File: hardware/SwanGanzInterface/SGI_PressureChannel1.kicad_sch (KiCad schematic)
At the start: 17 parts, among them U4 INA122D, U5 OPA2350

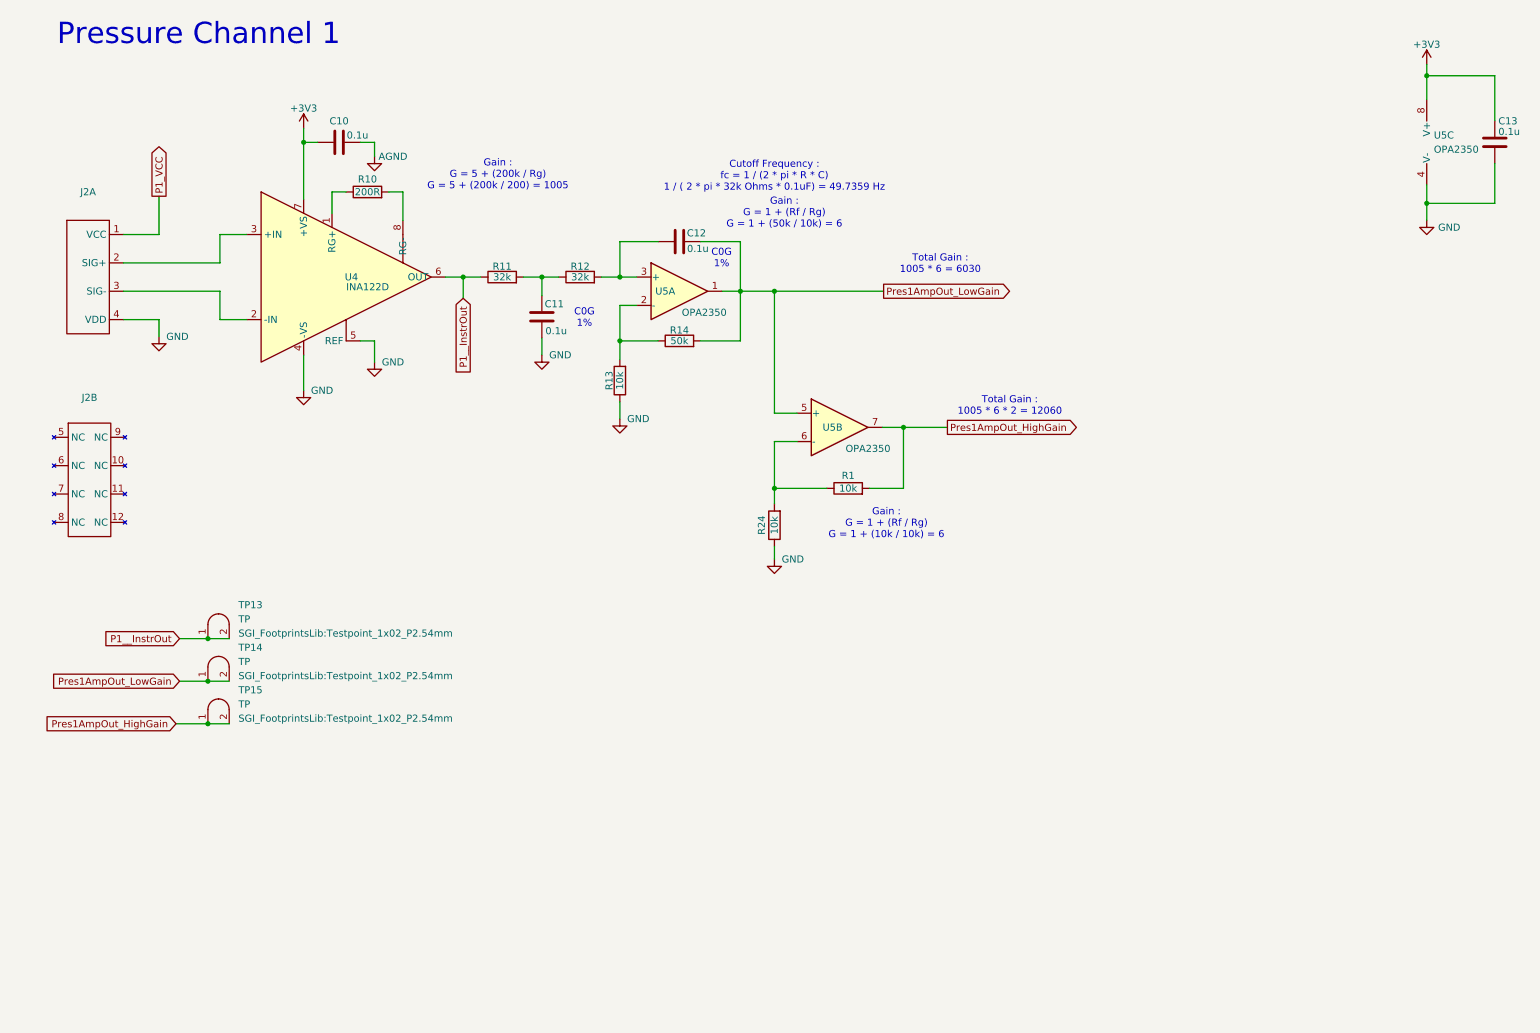
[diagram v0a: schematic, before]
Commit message: Routed Microcontroller Schematic Pins
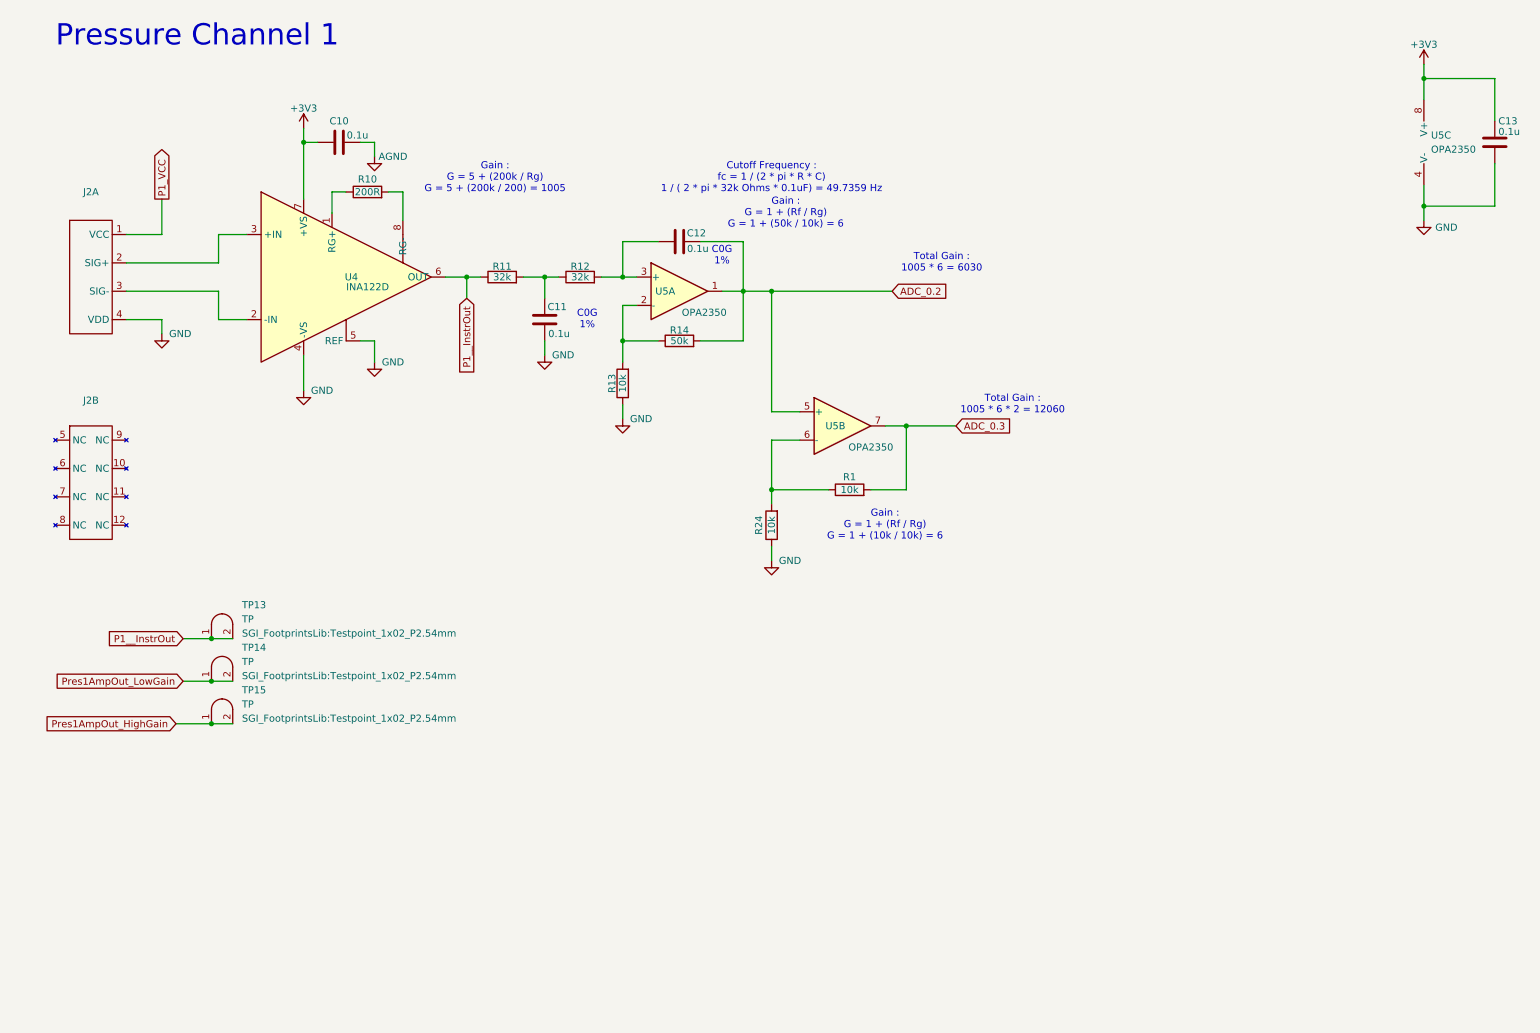
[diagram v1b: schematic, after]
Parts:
- C11, C12: footprint (none) -> Capacitor_SMD:C_1206_3216Metric
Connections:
- net Pres1AmpOut_HighGain: no longer R1.2, U5.7
- net Pres1AmpOut_LowGain: no longer C12.2, R14.2, U5.1, U5.5 (+)
- new net ADC_0.2: C12.2, R14.2, U5.1, U5.5 (+)
- new net ADC_0.3: R1.2, U5.7
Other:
- moved on the sheet: C11, J2A, J2B, R13, R24, TP13, TP14, TP15, U5B, U5C

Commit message: Added Test Points to the Outputs of Analog Circuits
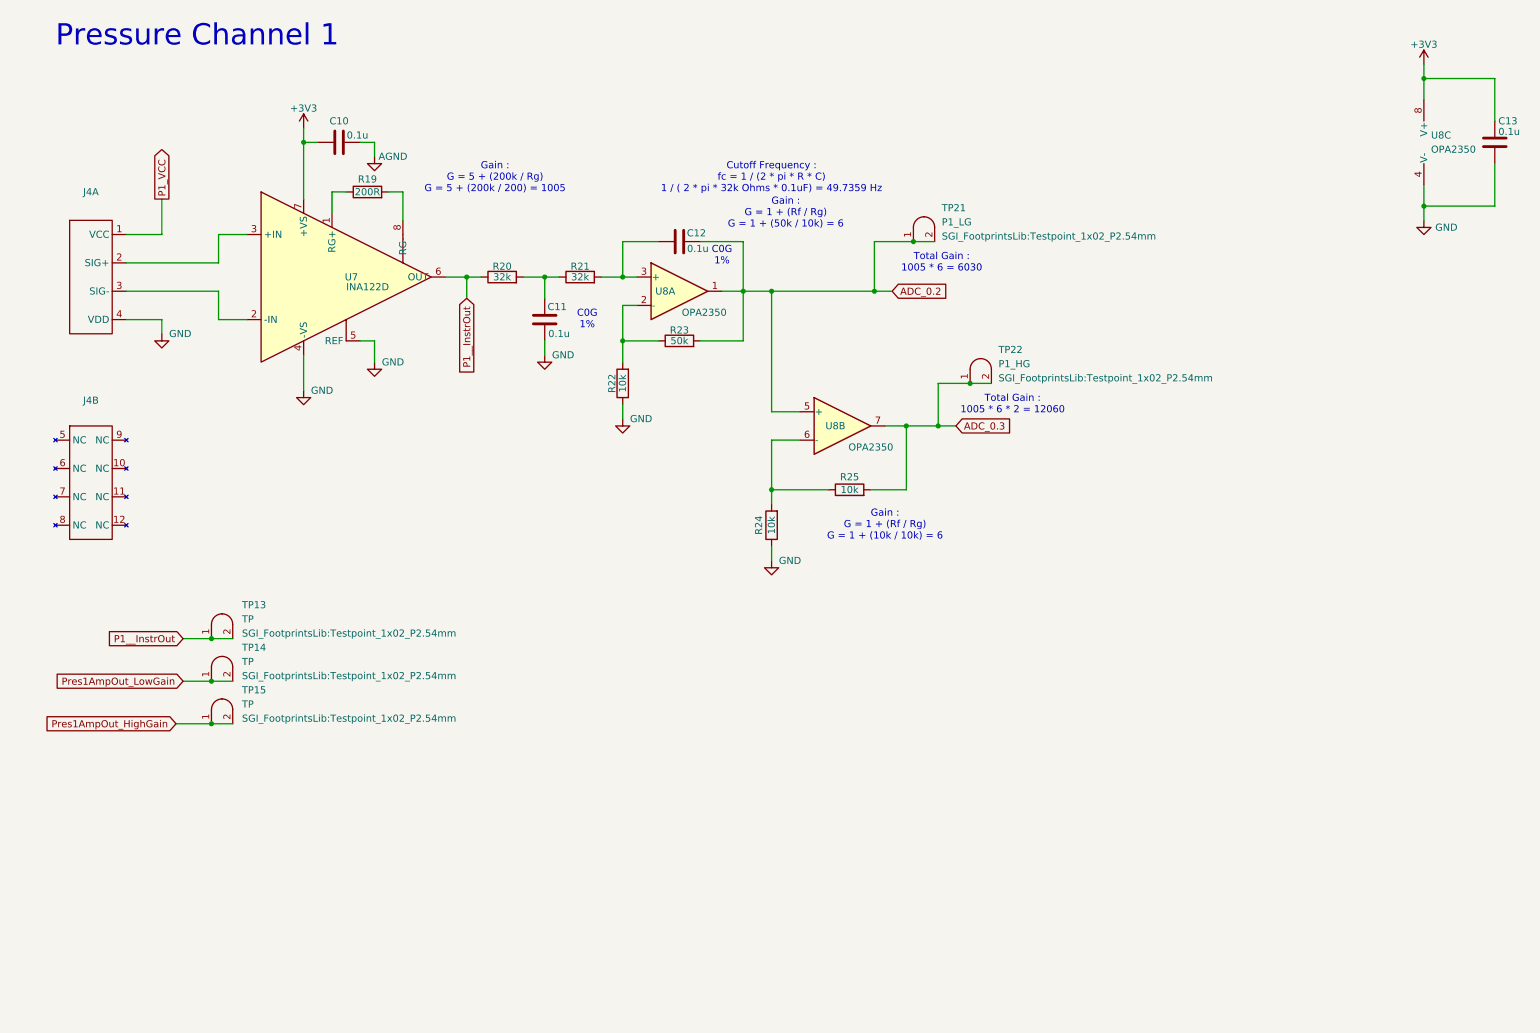
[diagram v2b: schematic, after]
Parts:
- added TP21: P1_LG, SGI_FootprintsLib:Testpoint_1x02_P2.54mm, symbol SGI_SymbolLib:Testpoint
- added TP22: P1_HG, SGI_FootprintsLib:Testpoint_1x02_P2.54mm, symbol SGI_SymbolLib:Testpoint
- C13: footprint (none) -> Capacitor_SMD:C_0603_1608Metric
- renumbered J2 to J4, R10 to R19, R11 to R20, R12 to R21, R13 to R22, R14 to R23, R1 to R25, U4 to U7, U5 to U8
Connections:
- net ADC_0.2: now also TP21.1 (A), TP21.2 (B)
- net ADC_0.3: now also TP22.1 (A), TP22.2 (B)

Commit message: Footprints for most parts, added LCD Driver
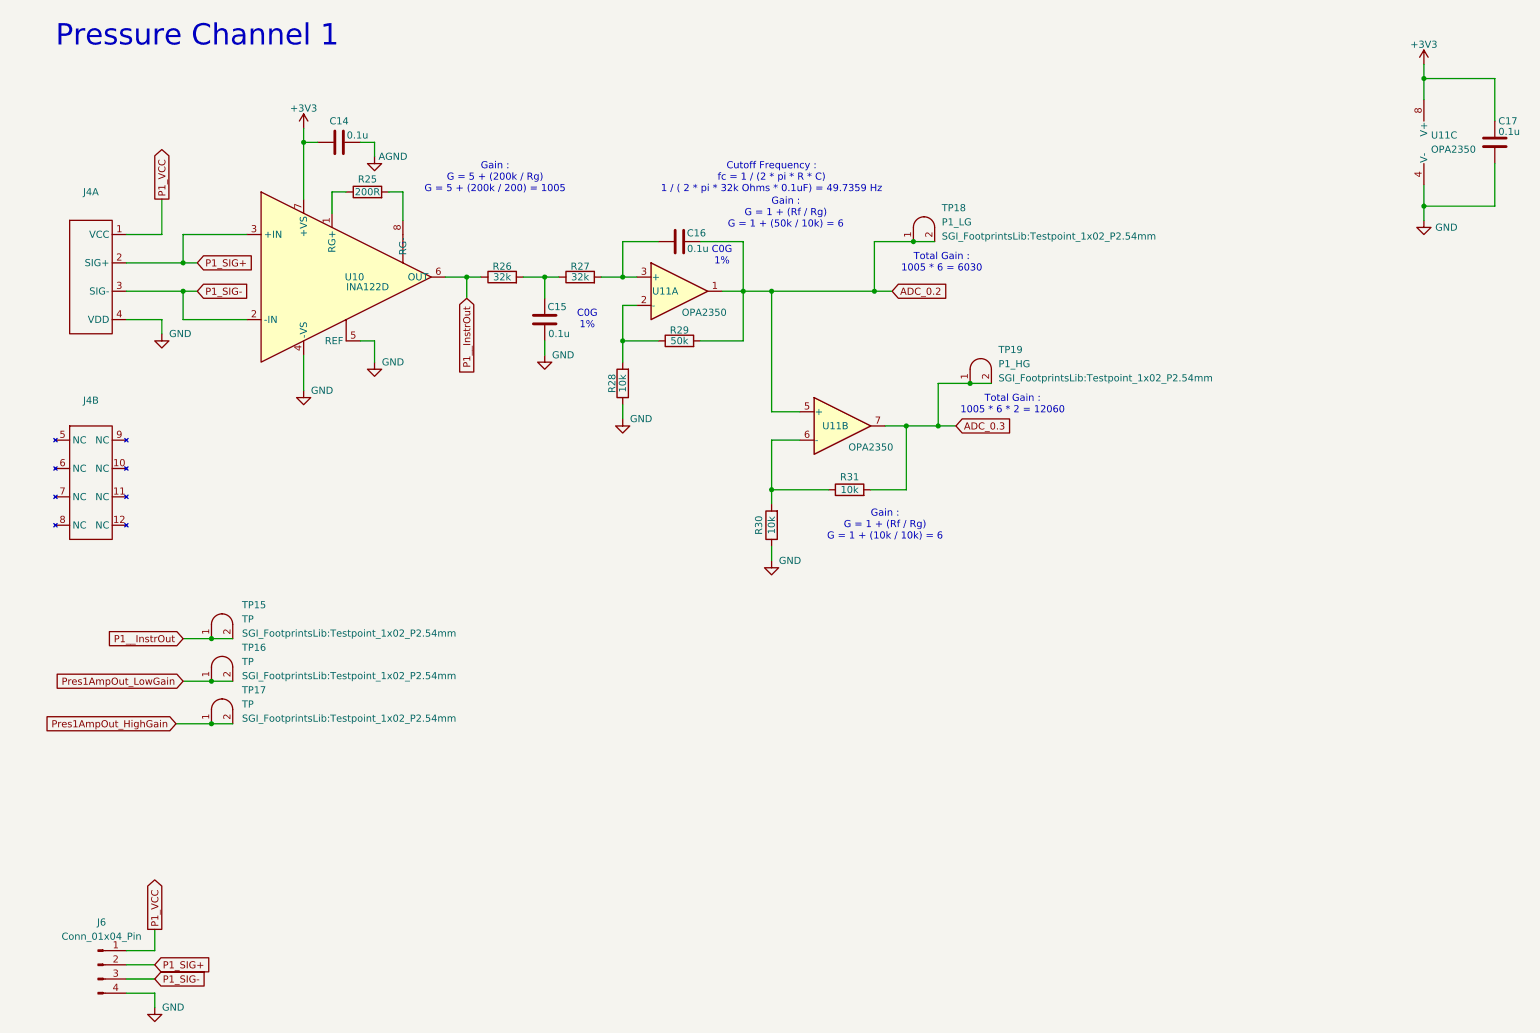
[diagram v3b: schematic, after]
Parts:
- added J6: Conn_01x04_Pin, Connector_PinSocket_2.54mm:PinSocket_1x04_P2.54mm_Vertical, symbol Connector:Conn_01x04_Pin
- R25: renamed from R19; footprint (none) -> Resistor_SMD:R_0603_1608Metric
- R26: renamed from R20; footprint (none) -> Resistor_SMD:R_0603_1608Metric
- R27: renamed from R21; footprint (none) -> Resistor_SMD:R_0603_1608Metric
- R28: renamed from R22; footprint (none) -> Resistor_SMD:R_0603_1608Metric
- R29: renamed from R23; footprint (none) -> Resistor_SMD:R_0603_1608Metric
- R30: renamed from R24; footprint (none) -> Resistor_SMD:R_0603_1608Metric
- R31: renamed from R25; footprint (none) -> Resistor_SMD:R_0603_1608Metric
- renumbered C10 to C14, C11 to C15, C12 to C16, C13 to C17, TP13 to TP15, TP14 to TP16, TP15 to TP17, TP21 to TP18, TP22 to TP19, U7 to U10, U8 to U11
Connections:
- net GND: now also J6.4 (Pin_4)
- net P1_VCC: now also J6.1 (Pin_1)
- net P1_SIG-: now reaches J4.3 (SIG-), U10.2 (-IN)
- net P1_SIG-: now also J6.3 (Pin_3)
- net P1_SIG+: now reaches J4.2 (SIG+), U10.3 (+IN)
- net P1_SIG+: now also J6.2 (Pin_2)

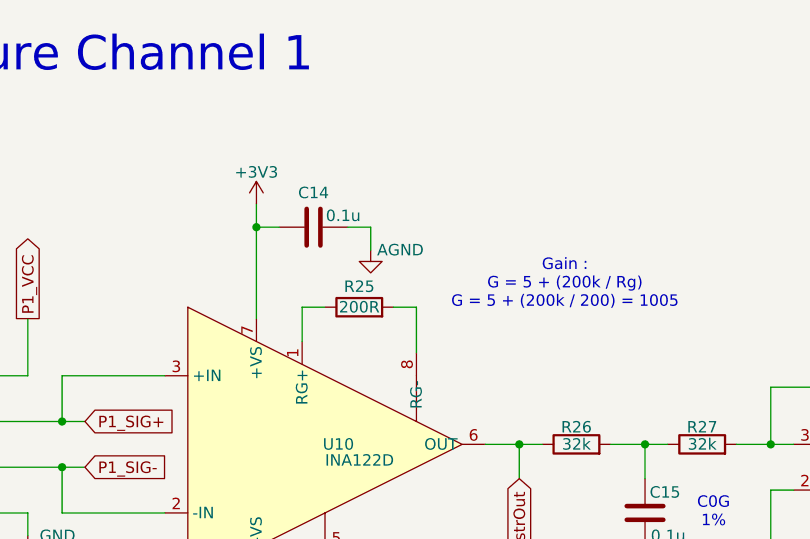
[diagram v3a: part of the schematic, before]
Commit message: Consolidated Grounds
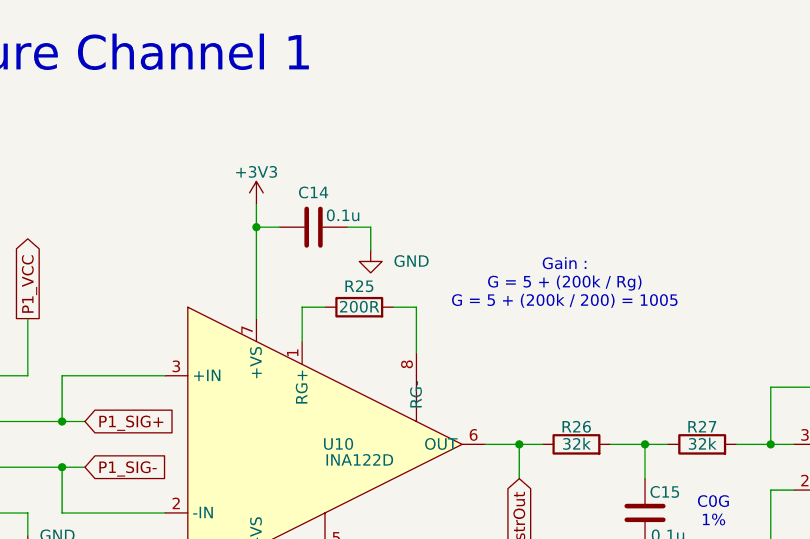
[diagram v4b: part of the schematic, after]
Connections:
- net AGND is gone; now on net GND: C14.1
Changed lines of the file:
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@@
+	)
+	(symbol
+		(lib_id "power:GNDA")
+		(at 74.93 40.64 0)
+		(unit 1)
+		(exclude_from_sim no)
+		(in_bom yes)
+		(on_board yes)
+		(dnp no)
+		(fields_autoplaced yes)
+		(property "Reference" "#PWR055"
+			(at 74.93 46.99 0)
+			(effects
+				(font
+					(size 1.27 1.27)
+				)
+				(hide yes)
+			)
+		)
+		(property "Value" "GND"
+			(at 77.47 41.9099 0)
+			(effects
+				(font
+					(size 1.27 1.27)
+				)
+				(justify left)
+			)
+		)
+		(property "Footprint" ""
+			(at 74.93 40.64 0)
+			(effects
+				(font
+					(size 1.27 1.27)
+				)
+				(hide yes)
+			)
+		)
+		(property "Datasheet" ""
+			(at 74.93 40.64 0)
+			(effects
+				(font
+					(size 1.27 1.27)
+				)
+				(hide yes)
+			)
+		)
+		(property "Description" "Power symbol creates a global label with name \"GNDA\" , analog ground"
+			(at 74.93 40.64 0)
+			(effects
+				(font
+					(size 1.27 1.27)
+				)
+				(hide yes)
+			)
+		)
+		(pin "1"
+		)
+		(instances
+			(project "SwanGanzInterface"
+				(path "/4e9a6e30-f660-472b-9696-bea1f34b4545/3d8fa9e7-4833-4941-a955-d778effe3e32"
+					(reference "#PWR055")
+					(unit 1)
+				)
+			)
+		)
 	)
 	(symbol
@@
 					(unit 1)
 				)
-			)
-		)
-	)
-	(symbol
-		(lib_id "power:GNDA")
-		(at 74.93 40.64 0)
-		(unit 1)
-		(exclude_from_sim no)
-		(in_bom yes)
-		(on_board yes)
-		(dnp no)
-		(property "Reference" "#PWR055"
-			(at 74.93 46.99 0)
-			(effects
-				(font
-					(size 1.27 1.27)
-				)
-				(hide yes)
-			)
-		)
-		(property "Value" "AGND"
-			(at 78.232 40.64 0)
-			(effects
-				(font
-					(size 1.27 1.27)
-				)
-			)
-		)
-		(property "Footprint" ""
-			(at 74.93 40.64 0)
-			(effects
-				(font
-					(size 1.27 1.27)
-				)
-				(hide yes)
-			)
-		)
-		(property "Datasheet" ""
-			(at 74.93 40.64 0)
-			(effects
-				(font
-					(size 1.27 1.27)
-				)
-				(hide yes)
-			)
-		)
-		(property "Description" "Power symbol creates a global label with name \"GNDA\" , analog ground"
-			(at 74.93 40.64 0)
-			(effects
-				(font
-					(size 1.27 1.27)
-				)
-				(hide yes)
-			)
-		)
-		(pin "1"
-		)
-		(instances
-			(project "SwanGanzInterface"
-				(path "/4e9a6e30-f660-472b-9696-bea1f34b4545/3d8fa9e7-4833-4941-a955-d778effe3e32"
-					(reference "#PWR055")
-					(unit 1)
-				)
